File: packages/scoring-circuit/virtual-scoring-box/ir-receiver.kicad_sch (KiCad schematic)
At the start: 3 parts, among them U13 TSOP38438

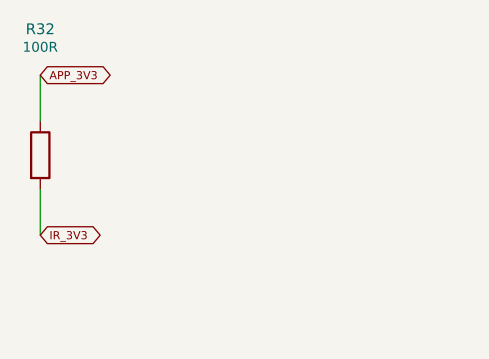
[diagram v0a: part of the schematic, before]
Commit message: feat(scoring-circuit): integrate isolated virtual-box processor supply
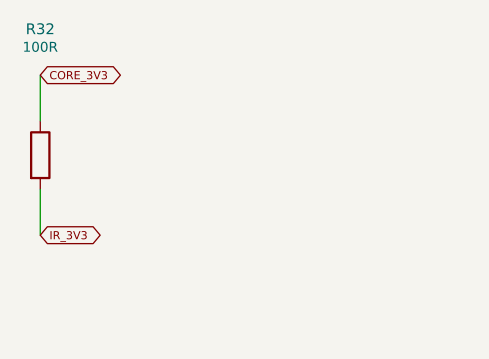
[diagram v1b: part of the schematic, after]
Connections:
- net APP_3V3 renamed CORE_3V3
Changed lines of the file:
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@@
-(kicad_sch (version 20250114) (generator "eeschema")
+(kicad_sch
+(version 20250114)
+(generator "eeschema")
 (paper "A3")
 (title_block (title "IR remote receiver") (rev "Integration draft") (comment 1 "NOT FOR FABRICATION"))
@@
 (symbol (lib_id "Device:R") (at 240.03 54.61 0) (unit 1) (in_bom yes) (on_board yes) (dnp no) (property "Reference" "R32" (at 240.03 40.61 0) (effects (font (size 1.2 1.2)))) (property "Value" "100R" (at 240.03 42.61 0) (effects (font (size 1.1 1.1)))) (property "Footprint" "Resistor_SMD:R_0603_1608Metric" (at 240.03 54.61 0) (effects (font (size 1 1)) (hide yes))) (pin "1") (pin "2") (property "Manufacturer" "YAGEO" (at 240.03 54.61 0) (effects (font (size 1 1)) (hide yes))) (property "MPN" "RC0603FR-07100RL" (at 240.03 54.61 0) (effects (font (size 1 1)) (hide yes))) (property "Datasheet" "https://www.yageogroup.com/component-documentation/download/specsheet/RC0603FR-07100RL" (at 240.03 54.61 0) (effects (font (size 1 1)) (hide yes))) (instances (project "virtual-scoring-box" (path "/20cc8167-128c-446a-a106-f942323e143f/bd387e31-6da9-4a92-aed7-12491d1f9509" (reference "R32") (unit 1)))))
 (wire (pts (xy 240.03 50.8) (xy 240.03 45.72)) (stroke (width 0) (type default)))
-(global_label "APP_3V3" (shape bidirectional) (at 240.03 45.72 0) (effects (font (size 0.9 0.9)) (justify left)) (property "Intersheetrefs" "" (at 240.03 45.72 0) (effects (font (size 1 1)) (hide yes))))
+(global_label "CORE_3V3" (shape bidirectional) (at 240.03 45.72 0) (effects (font (size 0.9 0.9)) (justify left)) (property "Intersheetrefs" "" (at 240.03 45.72 0) (effects (font (size 1 1)) (hide yes))))
 (wire (pts (xy 240.03 58.42) (xy 240.03 63.5)) (stroke (width 0) (type default)))
 (global_label "IR_3V3" (shape bidirectional) (at 240.03 63.5 0) (effects (font (size 0.9 0.9)) (justify left)) (property "Intersheetrefs" "" (at 240.03 63.5 0) (effects (font (size 1 1)) (hide yes))))
